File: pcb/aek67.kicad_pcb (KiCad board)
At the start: 2 copper layers, 304.8 x 100.4 mm, 154 parts, among them J1 AVR-ISP-6, K1 K_GRV, K10 K_9, K11 K_0, K12 K_MINUS, K13 K_EQUAL, K14 K_BACKSPACE, K15 K_PAGE_UP, K16 K_TAB, K17 K_Q, K18 K_W, K19 K_E, K2 K_1, K20 K_R, K21 K_T, K22 K_Y, K23 K_U, K24 K_I, K25 K_O, K26 K_P, K27 K_LBRC, K28 K_RBRC, K29 K_BSLSH, K3 K_2, K30 K_PAGE_DN, K31 K_CAPS_LOCK, K32 K_A, K33 K_S, K34 K_D, K35 K_F, K36 K_G, K37 K_H, K38 K_J, K39 K_K, K4 K_3, K40 K_L, K41 K_SEMIC, K42 K_QUOTE, K43 K_ENTER, K44 K_INSERT, K45 K_LSHIFT, K46 K_Z, K47 K_X, K48 K_C, K49 K_V, K5 K_4, K50 K_B, K51 K_N, K52 K_M, K53 K_COMMA, K54 K_DOT, K55 K_SLASH, K56 K_RSHIFT, K57 K_UP, K58 K_DELETE, K59 K_LCTRL, K6 K_5, K60 K_LAPP, K61 K_LALT, K62 K_SPC, K63 K_RALT, K64 K_RAPP, K65 K_LEFT, K66 K_DOWN, K67 K_RIGHT, K7 K_6, K8 K_7, K9 K_8, SW1 SW_PUSH, U1 ATmega32U4-AU, U2 PRTR5V0U2X, X1 XTAL_GND

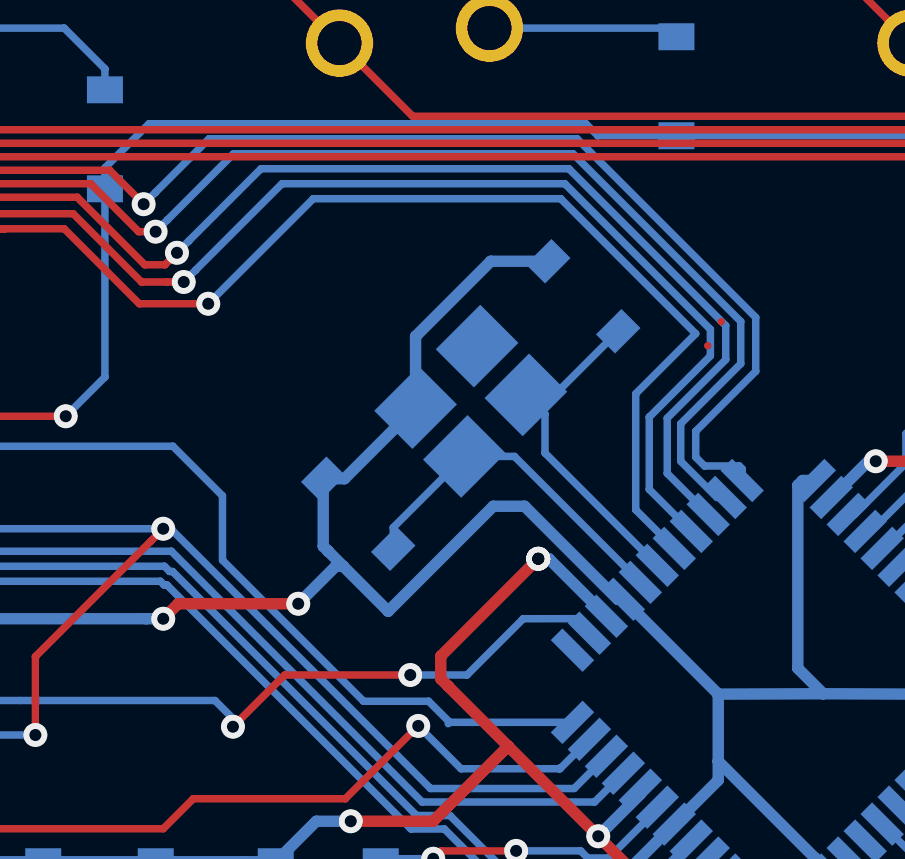
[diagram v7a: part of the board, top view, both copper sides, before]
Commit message: fixes some invisible tracks remains
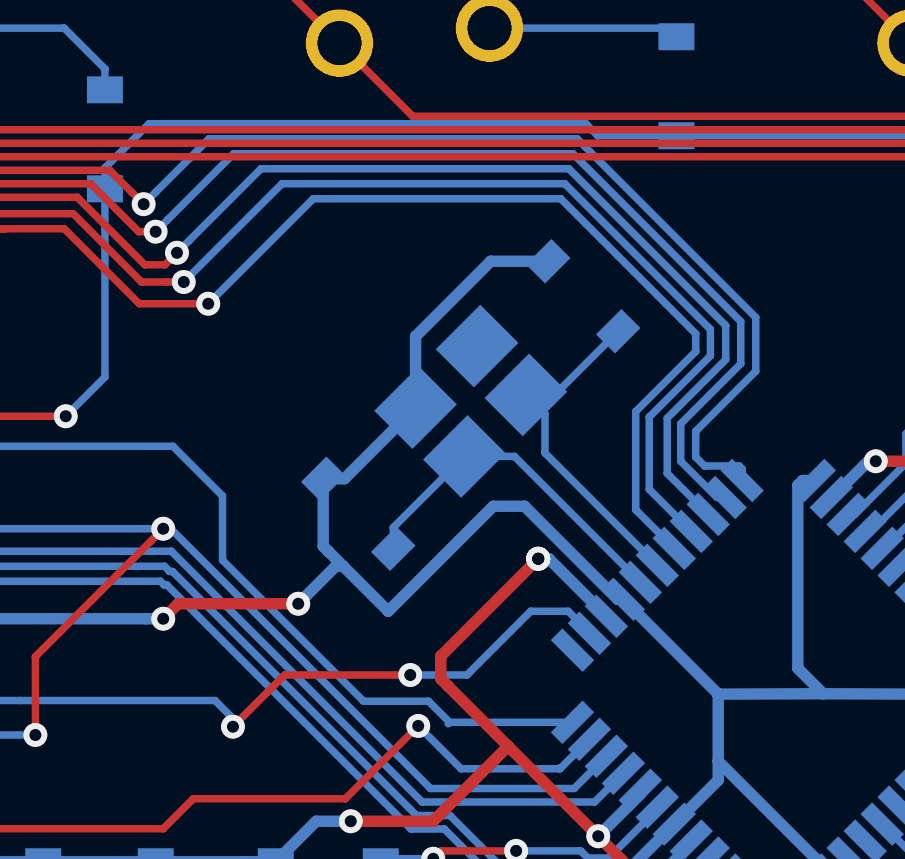
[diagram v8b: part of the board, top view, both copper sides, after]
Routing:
- net RST: track 75.3 -> 76.2 mm
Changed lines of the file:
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@@
   (via (at 206.234694 104.375001) (size 0.8) (drill 0.4) (layers F.Cu B.Cu) (net 77))
   (segment (start 200.323601 106.098893) (end 202.047493 104.375001) (width 0.25) (layer F.Cu) (net 77))
-  (segment (start 208.124999 104.375001) (end 210 102.5) (width 0.25) (layer B.Cu) (net 77))
-  (segment (start 206.234694 104.375001) (end 208.124999 104.375001) (width 0.25) (layer B.Cu) (net 77))
-  (segment (start 211.722641 102.498124) (end 210 102.5) (width 0.25) (layer B.Cu) (net 77))
+  (segment (start 211.5 102.25) (end 210.25 102.25) (width 0.25) (layer B.Cu) (net 77))
+  (segment (start 208.124999 104.375001) (end 206.234694 104.375001) (width 0.25) (layer B.Cu) (net 77))
+  (segment (start 210.25 102.25) (end 208.124999 104.375001) (width 0.25) (layer B.Cu) (net 77))
+  (segment (start 212.20675 102.95675) (end 211.5 102.25) (width 0.25) (layer B.Cu) (net 77))
+  (segment (start 212.20675 102.982233) (end 212.20675 102.95675) (width 0.25) (layer B.Cu) (net 77))
   (segment (start 211.641064 105.952082) (end 207.547918 105.952082) (width 0.25) (layer B.Cu) (net 78))
   (segment (start 207.547918 105.952082) (end 207.5 106) (width 0.25) (layer B.Cu) (net 78))
@@
   (segment (start 43.00625 86.75) (end 39.56875 83.3125) (width 0.25) (layer B.Cu) (net 81))
   (segment (start 53 86.75) (end 43.00625 86.75) (width 0.25) (layer B.Cu) (net 81))
-  (segment (start 215.035177 100.153806) (end 213.75 98.868629) (width 0.25) (layer B.Cu) (net 81))
   (via (at 199.5 92) (size 0.8) (drill 0.4) (layers F.Cu B.Cu) (net 81))
-  (segment (start 215.75 93) (end 211.25 88.5) (width 0.25) (layer B.Cu) (net 81))
-  (segment (start 213.75 95) (end 215.75 93) (width 0.25) (layer B.Cu) (net 81))
-  (segment (start 203.000004 88.5) (end 199.500004 92) (width 0.25) (layer B.Cu) (net 81))
-  (segment (start 211.25 88.5) (end 203.000004 88.5) (width 0.25) (layer B.Cu) (net 81))
-  (segment (start 213.75 98.868629) (end 213.75 95) (width 0.25) (layer B.Cu) (net 81))
-  (segment (start 199.500004 92) (end 199.5 92) (width 0.25) (layer B.Cu) (net 81))
   (segment (start 90.75 91) (end 92.25 89.5) (width 0.25) (layer F.Cu) (net 81))
   (segment (start 192.25 89.5) (end 192.75 89.5) (width 0.25) (layer F.Cu) (net 81))
@@
   (segment (start 197.20001 92) (end 194.70001 89.5) (width 0.25) (layer F.Cu) (net 81))
   (segment (start 199.5 92) (end 197.20001 92) (width 0.25) (layer F.Cu) (net 81))
+  (segment (start 203.000004 88.5) (end 199.500004 92) (width 0.25) (layer B.Cu) (net 81))
+  (segment (start 211.25 88.5) (end 203.000004 88.5) (width 0.25) (layer B.Cu) (net 81))
+  (segment (start 215.75 93) (end 211.25 88.5) (width 0.25) (layer B.Cu) (net 81))
+  (segment (start 199.500004 92) (end 199.5 92) (width 0.25) (layer B.Cu) (net 81))
+  (segment (start 215.035177 100.153806) (end 213.75 98.868629) (width 0.25) (layer B.Cu) (net 81))
+  (segment (start 215.75 93.59077) (end 215.75 93) (width 0.25) (layer B.Cu) (net 81))
+  (segment (start 213.75 95.59077) (end 215.75 93.59077) (width 0.25) (layer B.Cu) (net 81))
+  (segment (start 213.75 98.868629) (end 213.75 95.59077) (width 0.25) (layer B.Cu) (net 81))
   (segment (start 75.2875 45.2125) (end 71.4625 45.2125) (width 0.25) (layer F.Cu) (net 82))
   (segment (start 65.7625 39.5125) (end 65.7625 26.1625) (width 0.25) (layer F.Cu) (net 82))
@@
   (segment (start 80.05 64.2625) (end 80.05 73.7875) (width 0.25) (layer F.Cu) (net 82))
   (segment (start 89.575 97.6) (end 84.8125 102.3625) (width 0.25) (layer F.Cu) (net 82))
-  (segment (start 216.15002 93.40002) (end 216.150018 93.400018) (width 0.25) (layer F.Cu) (net 82))
   (segment (start 89.5 87.5) (end 89.575 97.6) (width 0.25) (layer F.Cu) (net 82))
   (segment (start 89.575 83.3125) (end 89.5 87.5) (width 0.25) (layer F.Cu) (net 82))
@@
   (segment (start 84.8125 37.5625) (end 84.8125 26.1625) (width 0.25) (layer F.Cu) (net 83))
   (segment (start 92.4625 45.2125) (end 84.8125 37.5625) (width 0.25) (layer F.Cu) (net 83))
-  (segment (start 216.60003 92.60003) (end 216.600028 92.600028) (width 0.25) (layer F.Cu) (net 83))
   (via (at 197.74628 89.598128) (size 0.8) (drill 0.4) (layers F.Cu B.Cu) (net 83))
   (segment (start 195.582518 88.000051) (end 197.180595 89.598128) (width 0.25) (layer F.Cu) (net 83))
@@
   (via (at 90.73734 89.98734) (size 0.8) (drill 0.4) (layers F.Cu B.Cu) (net 107))
   (via (at 198.683769 91.27499) (size 0.8) (drill 0.4) (layers F.Cu B.Cu) (net 107))
-  (segment (start 215.600862 99.58812) (end 214.20001 98.187268) (width 0.25) (layer B.Cu) (net 107))
-  (segment (start 214.20001 95.77717) (end 216.23859 93.73859) (width 0.25) (layer B.Cu) (net 107))
-  (segment (start 199.083768 90.874991) (end 198.683769 91.27499) (width 0.25) (layer B.Cu) (net 107))
-  (segment (start 216.23859 92.85218) (end 211.38641 88) (width 0.25) (layer B.Cu) (net 107))
-  (segment (start 201.958759 88) (end 199.083768 90.874991) (width 0.25) (layer B.Cu) (net 107))
-  (segment (start 216.23859 93.73859) (end 216.23859 92.85218) (width 0.25) (layer B.Cu) (net 107))
-  (segment (start 211.38641 88) (end 201.958759 88) (width 0.25) (layer B.Cu) (net 107))
-  (segment (start 214.20001 98.187268) (end 214.20001 95.77717) (width 0.25) (layer B.Cu) (net 107))
   (segment (start 197.27499 91.27499) (end 198.118084 91.27499) (width 0.25) (layer F.Cu) (net 107))
   (segment (start 91.72468 89) (end 195 89) (width 0.25) (layer F.Cu) (net 107))
@@
   (segment (start 195 89) (end 197.27499 91.27499) (width 0.25) (layer F.Cu) (net 107))
   (segment (start 90.73734 89.98734) (end 91.72468 89) (width 0.25) (layer F.Cu) (net 107))
+  (segment (start 214.20001 98.187268) (end 215.600862 99.58812) (width 0.25) (layer B.Cu) (net 107))
+  (segment (start 211.38641 88) (end 216.23859 92.85218) (width 0.25) (layer B.Cu) (net 107))
+  (segment (start 216.23859 93.73859) (end 214.20001 95.77717) (width 0.25) (layer B.Cu) (net 107))
+  (segment (start 216.23859 92.85218) (end 216.23859 93.73859) (width 0.25) (layer B.Cu) (net 107))
+  (segment (start 214.20001 95.77717) (end 214.20001 98.187268) (width 0.25) (layer B.Cu) (net 107))
+  (segment (start 201.958759 88) (end 211.38641 88) (width 0.25) (layer B.Cu) (net 107))
+  (segment (start 198.683769 91.27499) (end 201.958759 88) (width 0.25) (layer B.Cu) (net 107))
   (zone (net 100) (net_name GND) (layer B.Cu) (hatch edge 0.508)
     (connect_pads (clearance 0.3556))
